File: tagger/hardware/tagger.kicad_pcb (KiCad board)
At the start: 4 copper layers, 70 x 40 mm, 62 parts, among them J2 MICRO_SD_CARD, J4 SWD, J6 TETHER_POWER, J7 TETHER_DATA, J8 DISPLAY, J9 IO_CONN, SW1 RADIO_COMMISSION, SW24 BOOT0, SW26 NRST, U1 LSM6DS3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

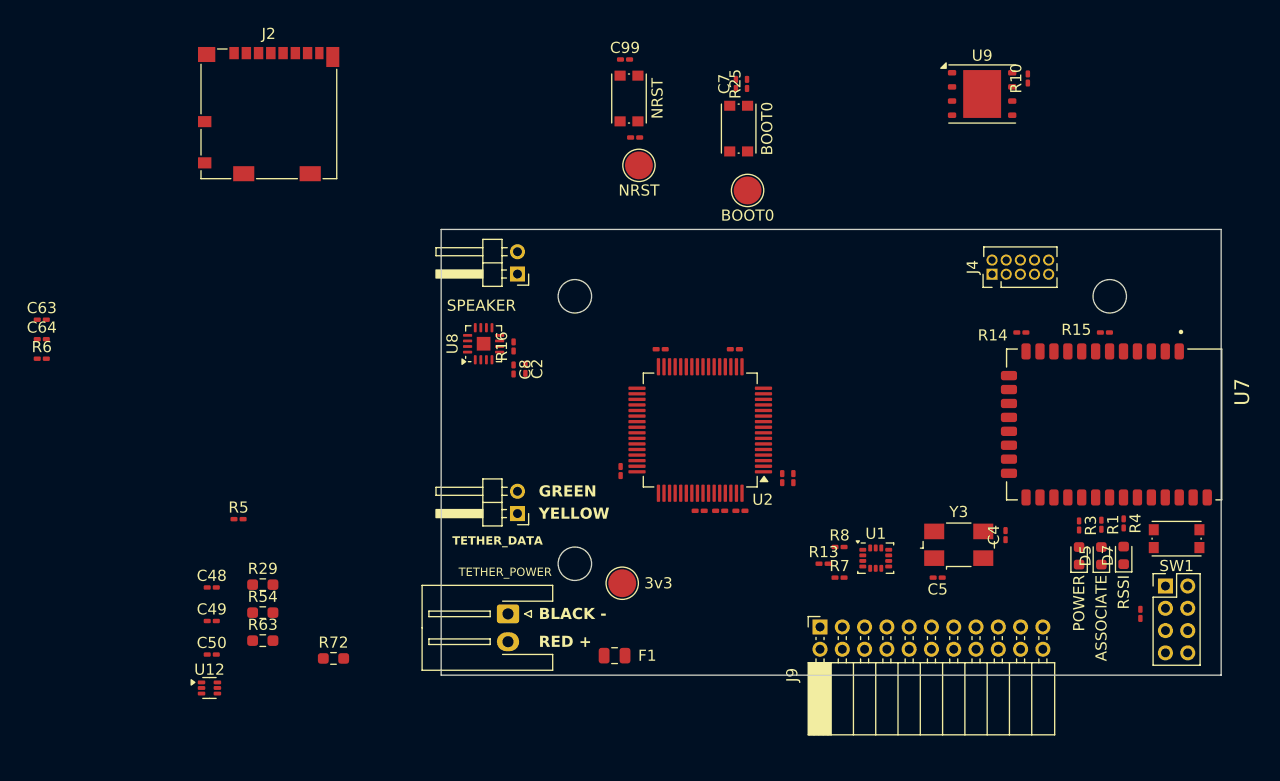
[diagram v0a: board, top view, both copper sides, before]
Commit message: feat: board routing and RS485 implementation
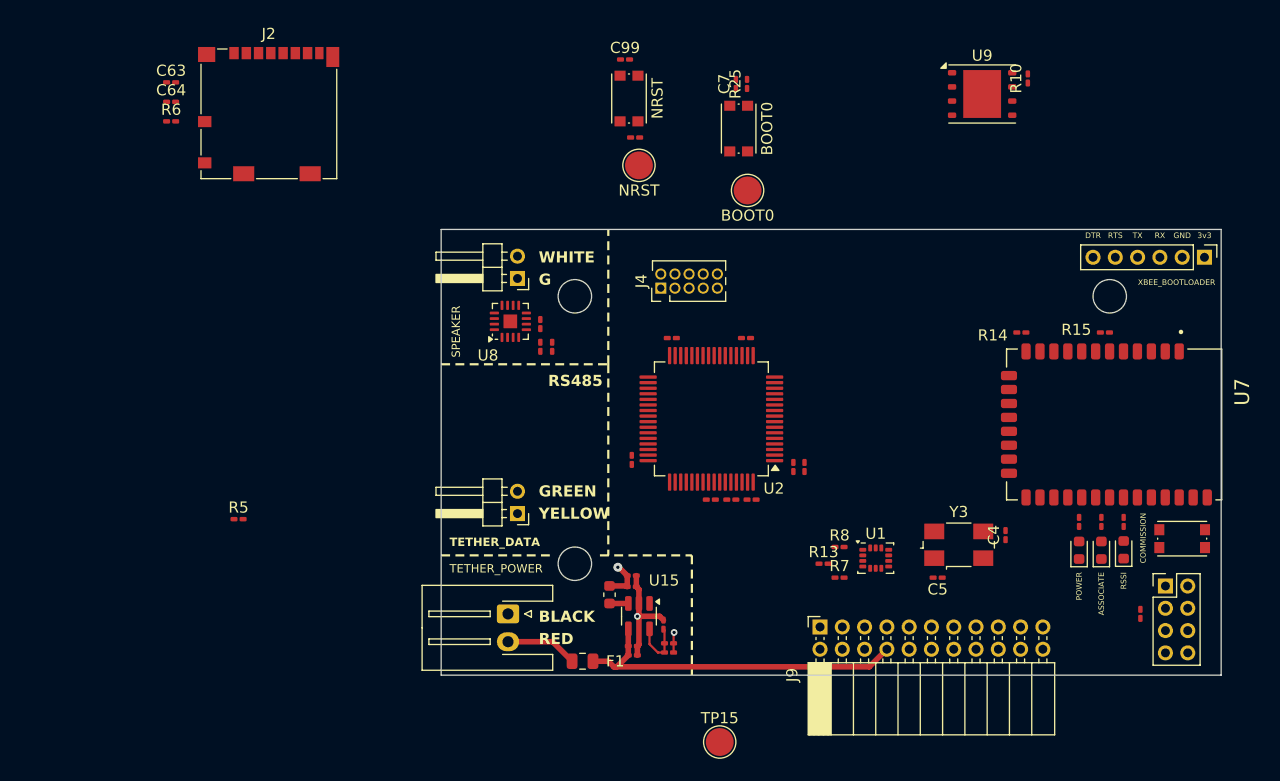
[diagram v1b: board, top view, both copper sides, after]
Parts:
- removed C48: 120pF, Capacitor_SMD:C_0201_0603Metric_Pad0.64x0.40mm_HandSolder
- removed C49: 22uf, Capacitor_SMD:C_0201_0603Metric_Pad0.64x0.40mm_HandSolder
- removed C50: 4.7uf, Capacitor_SMD:C_0201_0603Metric_Pad0.64x0.40mm_HandSolder
- removed R29: 442k, Resistor_SMD:R_0603_1608Metric_Pad0.98x0.95mm_HandSolder
- removed R54: 97.6k, Resistor_SMD:R_0603_1608Metric_Pad0.98x0.95mm_HandSolder
- removed R63: 499k, Resistor_SMD:R_0603_1608Metric_Pad0.98x0.95mm_HandSolder
- removed R72: 0R, Resistor_SMD:R_0603_1608Metric_Pad0.98x0.95mm_HandSolder
- removed TP14: 3v3, TestPoint:TestPoint_Pad_D2.5mm
- removed U12: TPS62A02DRL, Package_TO_SOT_SMD:SOT-563
- added C1: 10uF, Capacitor_SMD:C_0201_0603Metric_Pad0.64x0.40mm_HandSolder, F.Cu at (133.1, 109.1)
- added C10: 10uF, Capacitor_SMD:C_0201_0603Metric_Pad0.64x0.40mm_HandSolder, F.Cu at (133.2, 115.2)
- added C3: 10uF, Capacitor_SMD:C_0201_0603Metric_Pad0.64x0.40mm_HandSolder, F.Cu at (133.1, 108.1)
- added C6: 10uF, Capacitor_SMD:C_0201_0603Metric_Pad0.64x0.40mm_HandSolder, F.Cu at (136.4, 114.1)
- added C9: 0.1uF, Capacitor_SMD:C_0201_0603Metric_Pad0.64x0.40mm_HandSolder, F.Cu at (133.2, 114.4)
- added J1: XBEE_BOOTLOADER, Connector_PinHeader_2.00mm:PinHeader_1x06_P2.00mm_Vertical, F.Cu at (184.5, 79.5)
- added L1: 10uh, Inductor_SMD:L_0603_1608Metric, F.Cu at (131.1, 109.8)
- added R18: 20.0 k, Resistor_SMD:R_0201_0603Metric_Pad0.64x0.40mm_HandSolder, F.Cu at (135.9, 112.5)
- added R2: 61.9k, Resistor_SMD:R_0201_0603Metric_Pad0.64x0.40mm_HandSolder, F.Cu at (136.4, 115.0)
- added TP15: 3v3, TestPoint:TestPoint_Pad_D2.5mm, F.Cu at (141.0, 123.0)
- added U15: TPS560200, Package_TO_SOT_SMD:SOT-23-5, F.Cu at (133.8, 111.7)
- SW1: value RADIO_COMMISSION -> COMMISSION
- moved J4 29.8 mm to (135.7, 82.3)
- moved C63 24.3 mm to (91.8, 63.8)
- moved C64 24.3 mm to (91.8, 65.5)
- moved R6 24.3 mm to (91.8, 67.3)
- moved C8 3.15 mm to (124.9, 87.5)
- moved R16 3.13 mm to (124.9, 85.5)
- moved U8 3.13 mm to (122.2, 85.2)
- moved C2 3.11 mm to (126.0, 87.5)
- moved F1 2.92 mm to (128.7, 115.8)
- moved C100 1.41 mm to (143.4, 86.8)
- moved C101 1.41 mm to (136.7, 86.8)
- moved C102 1.41 mm to (133.1, 97.7)
- moved C103 1.41 mm to (143.9, 101.2)
- moved C66 1.41 mm to (148.6, 98.3)
- moved C68 1.41 mm to (147.6, 98.3)
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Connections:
- R12 pad 1: /Power/3v3_PG -> /3v3_PG
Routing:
- net VDD: track 0.00 -> 31.3 mm
- net GND: track 0.00 -> 9.64 mm, vias 0 -> 1
- net Net-(J6-Pin_2): track 0.00 -> 6.47 mm
- net +3.3V: track 0.00 -> 5.49 mm, vias 0 -> 2
- net /Power/FB: track 0.00 -> 5.15 mm
- net Net-(U15-PH): track 0.00 -> 1.69 mm
- removed copper zone on In1.Cu, net VDD
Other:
- board text added: "3v3"
- board text added: "BLACK"
- board text added: "DTR"
- board text added: "G"
- board text added: "GND"
- board text added: "RED"
- board text added: "RS485"
- board text added: "RTS"
- board text added: "RX"
- board text added: "TX"
- board text added: "WHITE"
- board text removed: "BLACK -"
- board text removed: "RED +"

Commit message: feat: more board layout
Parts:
- removed R12: 0R, Resistor_SMD:R_0201_0603Metric_Pad0.64x0.40mm_HandSolder
- added C104: 100nF, Capacitor_SMD:C_0201_0603Metric_Pad0.64x0.40mm_HandSolder, F.Cu at (123.0, 96.9)
- added R19: 500R, Resistor_SMD:R_0201_0603Metric_Pad0.64x0.40mm_HandSolder, F.Cu at (121.5, 98.2)
- added R20: 500R, Resistor_SMD:R_0201_0603Metric_Pad0.64x0.40mm_HandSolder, F.Cu at (117.5, 98.2)
- added R21: 130R, Resistor_SMD:R_0201_0603Metric_Pad0.64x0.40mm_HandSolder, F.Cu at (119.5, 98.2)
- added R26: 10k, Resistor_SMD:R_0201_0603Metric_Pad0.64x0.40mm_HandSolder, F.Cu at (143.2, 109.5)
- added R27: 10k, Resistor_SMD:R_0201_0603Metric_Pad0.64x0.40mm_HandSolder, F.Cu at (174.0, 86.4)
- added SW2: RESET, Button_Switch_SMD:SW_Push_1P1T_NO_CK_KMR2, F.Cu at (171.5, 84.5)
- added TP1: B, TestPoint:TestPoint_Bridge_Pitch2.54mm_Drill1.0mm, F.Cu at (126.2, 94.3)
- added TP16: VDD, TestPoint:TestPoint_Pad_D1.5mm, F.Cu at (130.8, 113.5)
- added TP2: A, TestPoint:TestPoint_Bridge_Pitch2.54mm_Drill1.0mm, F.Cu at (126.2, 97.8)
- added TP3: TX, TestPoint:TestPoint_Bridge_Pitch2.54mm_Drill1.0mm, F.Cu at (184.3, 86.0)
- added TP4: RX, TestPoint:TestPoint_Bridge_Pitch2.54mm_Drill1.0mm, F.Cu at (184.3, 82.8)
- added U4: ST3485EB, Package_SO:SOIC-8_3.9x4.9mm_P1.27mm, F.Cu at (119.5, 94.0)
- TP15, TP6, TP7: footprint TestPoint:TestPoint_Pad_D2.5mm -> TestPoint:TestPoint_Pad_D1.5mm
- moved J2 59.9 mm to (157.8, 84.2)
- moved C99 48.5 mm to (140.8, 109.5)
- moved SW26 48.2 mm to (141.2, 112.8)
- moved TP6 45.8 mm to (148.8, 114.5)
- moved C7 45.7 mm to (146.1, 109.5), turned to 180 degrees
- moved SW24 44.9 mm to (145.2, 112.8)
- moved R25 44.6 mm to (146.1, 108.5), turned to 180 degrees
- moved TP7 37.4 mm to (148.8, 110.5)
- moved U9 33.7 mm to (134.8, 80.8), turned to -90 degrees
- moved J4 22.1 mm to (133.2, 104.3)
- moved C5 18.6 mm to (149.8, 93.1), turned to 90 degrees
- moved TP15 15.7 mm to (135.8, 108.2)
- moved Y3 14.1 mm to (152.8, 95.0), turned to -90 degrees
- moved C4 14.0 mm to (153.6, 99.2), turned to 0 degrees
- moved U1 12.1 mm to (143.0, 105.1), turned to 180 degrees
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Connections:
- C99 pad 2: /DISPLAY_RST -> /SWD_RESET
- J2 pad 3: /~{SD_CS} -> /Peripherals/~{SD_CS}
- J4 pad 10: /DISPLAY_RST -> /SWD_RESET
- J7 pad 1: unconnected-(J7-Pin_1-Pad1) -> Net-(J7-Pin_1)
- J7 pad 2: unconnected-(J7-Pin_2-Pad2) -> Net-(J7-Pin_2)
- R15 pad 1: 3v3_PG -> Net-(R15-Pad1)
- SW26 pad 2: /DISPLAY_RST -> /SWD_RESET
- TP6 pad 1: /DISPLAY_RST -> /SWD_RESET
- U2 pad 10: unconnected-(U2-PC2-Pad10) -> /DISPLAY_D/C
- U2 pad 14: /DISPLAY_D/C -> /Peripherals/~{SD_CS}
- U2 pad 15: /~{DISPLAY_CS} -> /TETHER_RTS
- U2 pad 16: /Peripherals/SD_DETECT -> /TETHER_TX
- U2 pad 17: /~{SD_CS} -> /TETHER_RX
- U2 pad 2: /BTN_RELOAD -> /BTN_TRIGGER
- U2 pad 3: /9DOF_INT1 -> /BTN_MENU
- U2 pad 4: /9DOF_INT2 -> /BTN_RELOAD
- U2 pad 41: unconnected-(U2-PA8-Pad41) -> /~{DISPLAY_CS}
- U2 pad 51: /GRIP_DOUT -> unconnected-(U2-PC10-Pad51)
- U2 pad 52: /BTN_TRIGGER -> unconnected-(U2-PC11-Pad52)
- U2 pad 53: /BTN_MENU -> unconnected-(U2-PC12-Pad53)
- U2 pad 61: unconnected-(U2-PB8-Pad61) -> /9DOF_INT1
- U2 pad 62: unconnected-(U2-PB9-Pad62) -> /9DOF_INT2
- U2 pad 7: /DISPLAY_RST -> /SWD_RESET
- U2 pad 9: unconnected-(U2-PC1-Pad9) -> /GRIP_DOUT
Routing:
- net GND: track 9.64 -> 76.9 mm, vias 1 -> 17
- net +3.3V: track 5.49 -> 41.6 mm, vias 2 -> 14
- net /SWD_RESET: track 0.00 -> 23.1 mm
- net Net-(J7-Pin_1): track 0.00 -> 20.0 mm, vias 0 -> 1
- net Net-(J7-Pin_2): track 0.00 -> 16.9 mm
- net /RF/LED_RSSI: track 0.00 -> 16.4 mm, vias 0 -> 2
- net /RF/RF_UART_DIN: track 0.00 -> 14.5 mm
- net /RF/RF_UART_DOUT: track 0.00 -> 12.3 mm
- net /9DOF_INT2: track 0.00 -> 12.3 mm, vias 0 -> 2
- net /BOOT0: track 0.00 -> 9.26 mm
- net /9DOF_INT1: track 0.00 -> 8.58 mm, vias 0 -> 2
- net /SWD_SWDIO: track 0.00 -> 8.33 mm
- net /I2C_SDA: track 0.00 -> 7.62 mm
- net /SWD_SWO: track 0.00 -> 6.99 mm
- net /RF/SW_COMMISSION: track 0.00 -> 6.97 mm
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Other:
- board text added: "9DOF"
- board text added: "A"
- board text added: "FLASH"
- board text removed: "G"

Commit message: feat: various board routing changes
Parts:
- added TP5: GND, TestPoint:TestPoint_Bridge_Pitch2.54mm_Drill1.0mm, F.Cu at (148.8, 107.0)
- J1: footprint Connector_PinHeader_2.00mm:PinHeader_1x06_P2.00mm_Vertical -> Connector_PinHeader_2.54mm:PinHeader_1x06_P2.54mm_Vertical
- Y3: footprint Crystal:Crystal_SMD_0603-4Pin_6.0x3.5mm -> Crystal:Crystal_SMD_Abracon_ABM3B-4Pin_5.0x3.2mm
- moved C63 59.3 mm to (148.4, 81.2), turned to 180 degrees
- moved C64 59.0 mm to (148.4, 82.2), turned to 180 degrees
- moved R6 58.8 mm to (148.4, 83.2)
- moved R5 57.1 mm to (153.8, 107.5), turned to -90 degrees
- moved R10 33.0 mm to (139.8, 79.4), turned to 180 degrees
- moved C4 6.54 mm to (148.3, 95.4), turned to -90 degrees
- moved C66 2.03 mm to (148.5, 100.2)
- moved C68 2.03 mm to (147.5, 100.2)
- moved SW2 1.68 mm to (170.8, 83.0)
- moved J2 1.59 mm to (156.2, 84.2)
- moved C5 1.50 mm to (148.3, 93.2), turned to -90 degrees
- moved U9 1.33 mm to (135.7, 81.8)
- moved Y3 1.10 mm to (152.0, 94.2), turned to 180 degrees
- moved TP15 1.00 mm to (136.8, 108.2)
- moved TP4 0.50 mm to (184.2, 82.2)
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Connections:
- J8 pad 5: /DISPLAY_CS -> /~{DISPLAY_CS}
- J8 pad 8: /SPI_MOSI -> /SPI_PICO
- U15 pad 1: VDD -> unconnected-(U15-EN-Pad1)
- U2 pad 11: unconnected-(U2-PC3-Pad11) -> /DISPLAY_RST
- U2 pad 41: /~{DISPLAY_CS} -> unconnected-(U2-PA8-Pad41)
- U2 pad 57: unconnected-(U2-PB5-Pad57) -> /GRIP_DOUT
- U2 pad 9: /GRIP_DOUT -> /~{DISPLAY_CS}
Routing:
- net /SPI_PICO: track 0.00 -> 83.0 mm, vias 0 -> 2
- net /SPI_SCLK: track 0.00 -> 75.7 mm, vias 0 -> 3
- net /RF/RF_UART_RTS: track 0.00 -> 75.5 mm, vias 0 -> 3
- net /DISPLAY_D/C: track 0.00 -> 55.2 mm, vias 0 -> 1
- net /RF/RF_UART_DOUT: track 12.3 -> 66.9 mm, vias 0 -> 2
- net /~{DISPLAY_CS}: track 0.00 -> 53.9 mm, vias 0 -> 1
- net /DISPLAY_RST: track 0.00 -> 51.2 mm, vias 0 -> 2
- net /RF/RF_UART_DIN: track 14.5 -> 65.0 mm, vias 0 -> 2
- net /RF/RF_UART_CTS: track 0.00 -> 49.3 mm, vias 0 -> 2
- net /TETHER_TX: track 0.00 -> 33.1 mm, vias 0 -> 4
- net /TETHER_RTS: track 0.00 -> 32.8 mm, vias 0 -> 3
- net GND: track 76.9 -> 107.7 mm, vias 17 -> 25
- net /SPI_POCI: track 0.00 -> 29.6 mm, vias 0 -> 3
- net /TETHER_RX: track 0.00 -> 26.6 mm, vias 0 -> 2
- net /Peripherals/~{SD_CS}: track 0.00 -> 17.8 mm, vias 0 -> 2
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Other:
- board text added: "EMIT."
- board text added: "LASER"
- board text added: "RECOIL"
- board text added: "REV 2: - Rotate stm32 90deg - put XBee stm32 and flash are - shift SD card to right OR swap stm32 to SD card position move RF module to stm32 position mode SD card to RF module position"
- board text added: "SD"
- board text added: "XBEE"
